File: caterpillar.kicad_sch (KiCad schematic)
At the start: 31 parts, among them J1 Conn_ARM_JTAG_SWD_10, M1 Conn_01x02_Pin, M2 *, M3 Conn_01x02_Pin, U1 STBB1-APUR, U2 ASM330LHHTR, U3 DRV8212P, U4 ADP2503ACPZ-3.3-R7, U6 max5419leta+T

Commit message: library: extract AN54LQ-P15 module from design files into a real library
The Raytac AN54LQ-P15 (nRF54L15) module existed only as embedded copies
in the schematic/board; its source library was a broken absolute path
on another machine. Extract it into library/AN54LQ-P15/ per the
project's component layout:

- footprint: pulled from the placed M2 via the pcbnew API (position
  reset, REF**, nets/sheet path stripped), 41 pads verified
- symbol: extracted from the schematic's lib_symbols, wrapped as a
  KiCad 10 symbol library, Footprint property fully qualified
- both lib tables gain an AN54LQ-P15 entry; nickname matches existing
  design references, so no design-file changes needed
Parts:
- U1: footprint STBB1_APUR:SON_B1-APUR_STM -> SON_B1-APUR_STM
- U2: footprint ASM330LHHTR:LGA-14L_2P5X3X0P83_STM -> LGA-14L_2P5X3X0P83_STM
- U4: footprint ADP2503ACPZ_3_3_R7:CP_10_9_ADI -> CP_10_9_ADI
- U6: footprint max5419:21-0137_T833&plus_2_MXM-L -> 21-0137_T833+2_MXM
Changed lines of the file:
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@@
 			)
 		)
-		(property "Description" ""
+		(property "Description" "Inductor, small symbol"
 			(at 40.64 149.86 90)
 			(hide yes)
@@
 			)
 		)
-		(property "Description" ""
+		(property "Description" "Generic connector, single row, 01x01, script generated"
 			(at 238.76 143.51 0)
 			(hide yes)
@@
 			)
 		)
-		(property "Description" ""
+		(property "Description" "Unpolarized capacitor, small symbol"
 			(at 220.98 124.46 0)
 			(hide yes)
@@
 			)
 		)
-		(property "Description" ""
+		(property "Description" "Unpolarized capacitor, small symbol"
 			(at 44.45 142.24 0)
 			(hide yes)
@@
 			)
 		)
-		(property "Description" ""
+		(property "Description" "Resistor, small US symbol"
 			(at 213.36 125.73 0)
 			(hide yes)
@@
 			)
 		)
-		(property "Description" ""
+		(property "Description" "Generic connector, single row, 01x02, script generated"
 			(at 17.78 154.94 0)
 			(hide yes)
@@
 			)
 		)
-		(property "Description" ""
+		(property "Description" "Unpolarized capacitor, small symbol"
 			(at 138.43 144.78 0)
 			(hide yes)
@@
 			)
 		)
-		(property "Description" ""
+		(property "Description" "Generic connector, single row, 01x01, script generated"
 			(at 238.76 146.05 0)
 			(hide yes)
@@
 			)
 		)
-		(property "Description" ""
+		(property "Description" "Generic connector, single row, 01x02, script generated"
 			(at 24.13 92.71 0)
 			(hide yes)
@@
 			)
 		)
-		(property "Description" ""
+		(property "Description" "Inductor, small symbol"
 			(at 137.16 138.43 90)
 			(hide yes)
@@
 			)
 		)
-		(property "Description" ""
+		(property "Description" "Resistor, small US symbol"
 			(at 231.14 128.27 0)
 			(hide yes)
@@
 			)
 		)
-		(property "Description" ""
+		(property "Description" "Unpolarized capacitor, small symbol"
 			(at 257.81 87.63 0)
 			(hide yes)
@@
 			)
 		)
-		(property "Footprint" "max5419:21-0137_T833&plus_2_MXM-L"
+		(property "Footprint" "21-0137_T833+2_MXM"
 			(at 125.73 179.07 0)
 			(hide yes)
@@
 			)
 		)
-		(property "Description" ""
+		(property "Description" "Unpolarized capacitor, small symbol"
 			(at 261.62 87.63 0)
 			(hide yes)
@@
 			)
 		)
-		(property "Description" ""
+		(property "Description" "Unpolarized capacitor, small symbol"
 			(at 142.24 127 0)
 			(hide yes)
@@
 			)
 		)
-		(property "Description" ""
+		(property "Description" "Generic connector, single row, 01x01, script generated"
 			(at 238.76 148.59 0)
 			(hide yes)
@@
 			)
 		)
-		(property "Description" ""
+		(property "Description" "Unpolarized capacitor, small symbol"
 			(at 16.51 132.08 0)
 			(hide yes)
@@
 			)
 		)
-		(property "Footprint" "ASM330LHHTR:LGA-14L_2P5X3X0P83_STM"
+		(property "Footprint" "LGA-14L_2P5X3X0P83_STM"
 			(at 212.09 69.85 0)
 			(hide yes)
@@
 			)
 		)
-		(property "Footprint" "ADP2503ACPZ_3_3_R7:CP_10_9_ADI"
+		(property "Footprint" "CP_10_9_ADI"
 			(at 48.26 144.78 0)
 			(hide yes)
@@
 			)
 		)
-		(property "Footprint" "STBB1_APUR:SON_B1-APUR_STM"
+		(property "Footprint" "SON_B1-APUR_STM"
 			(at 144.78 132.08 0)
 			(hide yes)
@@
 			)
 		)
-		(property "Description" ""
+		(property "Description" "Resistor, small US symbol"
 			(at 238.76 128.27 0)
 			(hide yes)
@@
 			)
 		)
-		(property "Description" ""
+		(property "Description" "Generic connector, single row, 01x01, script generated"
 			(at 238.76 151.13 0)
 			(hide yes)
@@
 			)
 		)
-		(property "Description" ""
+		(property "Description" "Unpolarized capacitor, small symbol"
 			(at 125.73 175.26 0)
 			(hide yes)

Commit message: replaced L5 with large inductor footprints. Fixed some warning about footprint links. Using M (largest pads) footprints for ICs now
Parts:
- L5: footprint Inductor_SMD:L_0402_1005Metric -> VLCF4020T-2R2N1R7:VLCF4020
- U1: footprint SON_B1-APUR_STM -> STBB1_APUR:SON_B1-APUR_STM-M
- U2: footprint LGA-14L_2P5X3X0P83_STM -> ASM330LHHTR:LGA-14L_2P5X3X0P83_STM-L
- U4: footprint CP_10_9_ADI -> ADP2503ACPZ_3_3_R7:CP_10_9_ADI-M
- U6: footprint 21-0137_T833+2_MXM -> max5419:21-0137_T833&plus_2_MXM-M
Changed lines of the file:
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@@
 			)
 		)
-		(property "Footprint" "Inductor_SMD:L_0402_1005Metric"
+		(property "Footprint" "VLCF4020T-2R2N1R7:VLCF4020"
 			(at 137.16 138.43 0)
 			(hide yes)
@@
 			)
 		)
-		(property "Footprint" "21-0137_T833+2_MXM"
+		(property "Footprint" "max5419:21-0137_T833&plus_2_MXM-M"
 			(at 125.73 179.07 0)
 			(hide yes)
@@
 			)
 		)
-		(property "Footprint" "LGA-14L_2P5X3X0P83_STM"
+		(property "Footprint" "ASM330LHHTR:LGA-14L_2P5X3X0P83_STM-L"
 			(at 212.09 69.85 0)
 			(hide yes)
@@
 			)
 		)
-		(property "Footprint" "CP_10_9_ADI"
+		(property "Footprint" "ADP2503ACPZ_3_3_R7:CP_10_9_ADI-M"
 			(at 48.26 144.78 0)
 			(hide yes)
@@
 			)
 		)
-		(property "Footprint" "SON_B1-APUR_STM"
+		(property "Footprint" "STBB1_APUR:SON_B1-APUR_STM-M"
 			(at 144.78 132.08 0)
 			(hide yes)

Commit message: replaced all 0402 footprints with 0603
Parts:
- C1, C10, C11, C12, C2, C3, C5, C6, C7, C8, C9: footprint Capacitor_SMD:C_0402_1005Metric -> Capacitor_SMD:C_0603_1608Metric
- L1, L6: footprint Inductor_SMD:L_0402_1005Metric -> Inductor_SMD:L_0603_1608Metric
- R3, R4, R8: footprint Resistor_SMD:R_0402_1005Metric -> Resistor_SMD:R_0603_1608Metric
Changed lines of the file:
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@@
 			)
 		)
-		(property "Footprint" "Inductor_SMD:L_0402_1005Metric"
+		(property "Footprint" "Inductor_SMD:L_0603_1608Metric"
 			(at 40.64 149.86 0)
 			(hide yes)
@@
 			)
 		)
-		(property "Footprint" "Capacitor_SMD:C_0402_1005Metric"
+		(property "Footprint" "Capacitor_SMD:C_0603_1608Metric"
 			(at 220.98 124.46 0)
 			(hide yes)
@@
 			)
 		)
-		(property "Footprint" "Capacitor_SMD:C_0402_1005Metric"
+		(property "Footprint" "Capacitor_SMD:C_0603_1608Metric"
 			(at 44.45 142.24 0)
 			(hide yes)
@@
 			)
 		)
-		(property "Footprint" "Resistor_SMD:R_0402_1005Metric"
+		(property "Footprint" "Resistor_SMD:R_0603_1608Metric"
 			(at 213.36 125.73 0)
 			(hide yes)
@@
 			)
 		)
-		(property "Footprint" "Capacitor_SMD:C_0402_1005Metric"
+		(property "Footprint" "Capacitor_SMD:C_0603_1608Metric"
 			(at 138.43 144.78 0)
 			(hide yes)
@@
 			)
 		)
-		(property "Footprint" "Capacitor_SMD:C_0402_1005Metric"
+		(property "Footprint" "Capacitor_SMD:C_0603_1608Metric"
 			(at 72.39 35.56 0)
 			(hide yes)
@@
 			)
 		)
-		(property "Footprint" "Capacitor_SMD:C_0402_1005Metric"
+		(property "Footprint" "Capacitor_SMD:C_0603_1608Metric"
 			(at 66.04 35.56 0)
 			(hide yes)
@@
 			)
 		)
-		(property "Footprint" "Capacitor_SMD:C_0402_1005Metric"
+		(property "Footprint" "Capacitor_SMD:C_0603_1608Metric"
 			(at 58.42 35.56 0)
 			(hide yes)
@@
 			)
 		)
-		(property "Footprint" "Resistor_SMD:R_0402_1005Metric"
+		(property "Footprint" "Resistor_SMD:R_0603_1608Metric"
 			(at 231.14 128.27 0)
 			(hide yes)
@@
 			)
 		)
-		(property "Footprint" "Capacitor_SMD:C_0402_1005Metric"
+		(property "Footprint" "Capacitor_SMD:C_0603_1608Metric"
 			(at 257.81 87.63 0)
 			(hide yes)
@@
 			)
 		)
-		(property "Footprint" "Capacitor_SMD:C_0402_1005Metric"
+		(property "Footprint" "Capacitor_SMD:C_0603_1608Metric"
 			(at 261.62 87.63 0)
 			(hide yes)
@@
 			)
 		)
-		(property "Footprint" "Inductor_SMD:L_0402_1005Metric"
+		(property "Footprint" "Inductor_SMD:L_0603_1608Metric"
 			(at 114.3 63.5 0)
 			(hide yes)
@@
 			)
 		)
-		(property "Footprint" "Capacitor_SMD:C_0402_1005Metric"
+		(property "Footprint" "Capacitor_SMD:C_0603_1608Metric"
 			(at 142.24 127 0)
 			(hide yes)
@@
 			)
 		)
-		(property "Footprint" "Capacitor_SMD:C_0402_1005Metric"
+		(property "Footprint" "Capacitor_SMD:C_0603_1608Metric"
 			(at 16.51 132.08 0)
 			(hide yes)
@@
 			)
 		)
-		(property "Footprint" "Resistor_SMD:R_0402_1005Metric"
+		(property "Footprint" "Resistor_SMD:R_0603_1608Metric"
 			(at 238.76 128.27 0)
 			(hide yes)
@@
 			)
 		)
-		(property "Footprint" "Capacitor_SMD:C_0402_1005Metric"
+		(property "Footprint" "Capacitor_SMD:C_0603_1608Metric"
 			(at 125.73 175.26 0)
 			(hide yes)

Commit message: reorganized design a lot for better space organization
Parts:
- removed 3.3V1, GND2, SCL1, SDA1: Conn_01x01_Pin, Connector_Wire:SolderWirePad_1x01_SMD_1x2mm, symbol Connector:Conn_01x01_Pin
- removed M1: Conn_01x02_Pin, Connector_PinHeader_2.00mm:PinHeader_1x02_P2.00mm_Vertical, symbol Connector:Conn_01x02_Pin
- removed M3: Conn_01x02_Pin, Connector_PinHeader_2.54mm:PinHeader_1x02_P2.54mm_Vertical, symbol Connector:Conn_01x02_Pin
- added J2: SM02B-SRSS-TB_LF__SN_, SM02B-SRSS-TB:SM02BSRSSTBLFSN, symbol SM02B-SRSS-TB:SM02B-SRSS-TB_LF__SN_
- added J3, J4: Castellated_2PTH_P1.27mm, Castellated_2PTH_P1.27mm:Castellated_2PTH_P1.27mm, symbol Castellated_2PTH_P1.27mm:Castellated_2PTH_P1.27mm
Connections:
- net +BATT: now also J2.1
- net GND: now also J2.2
- net OUT1: now also J3.1
- net OUT2: now also J4.1
- no-connect marks 5 -> 7

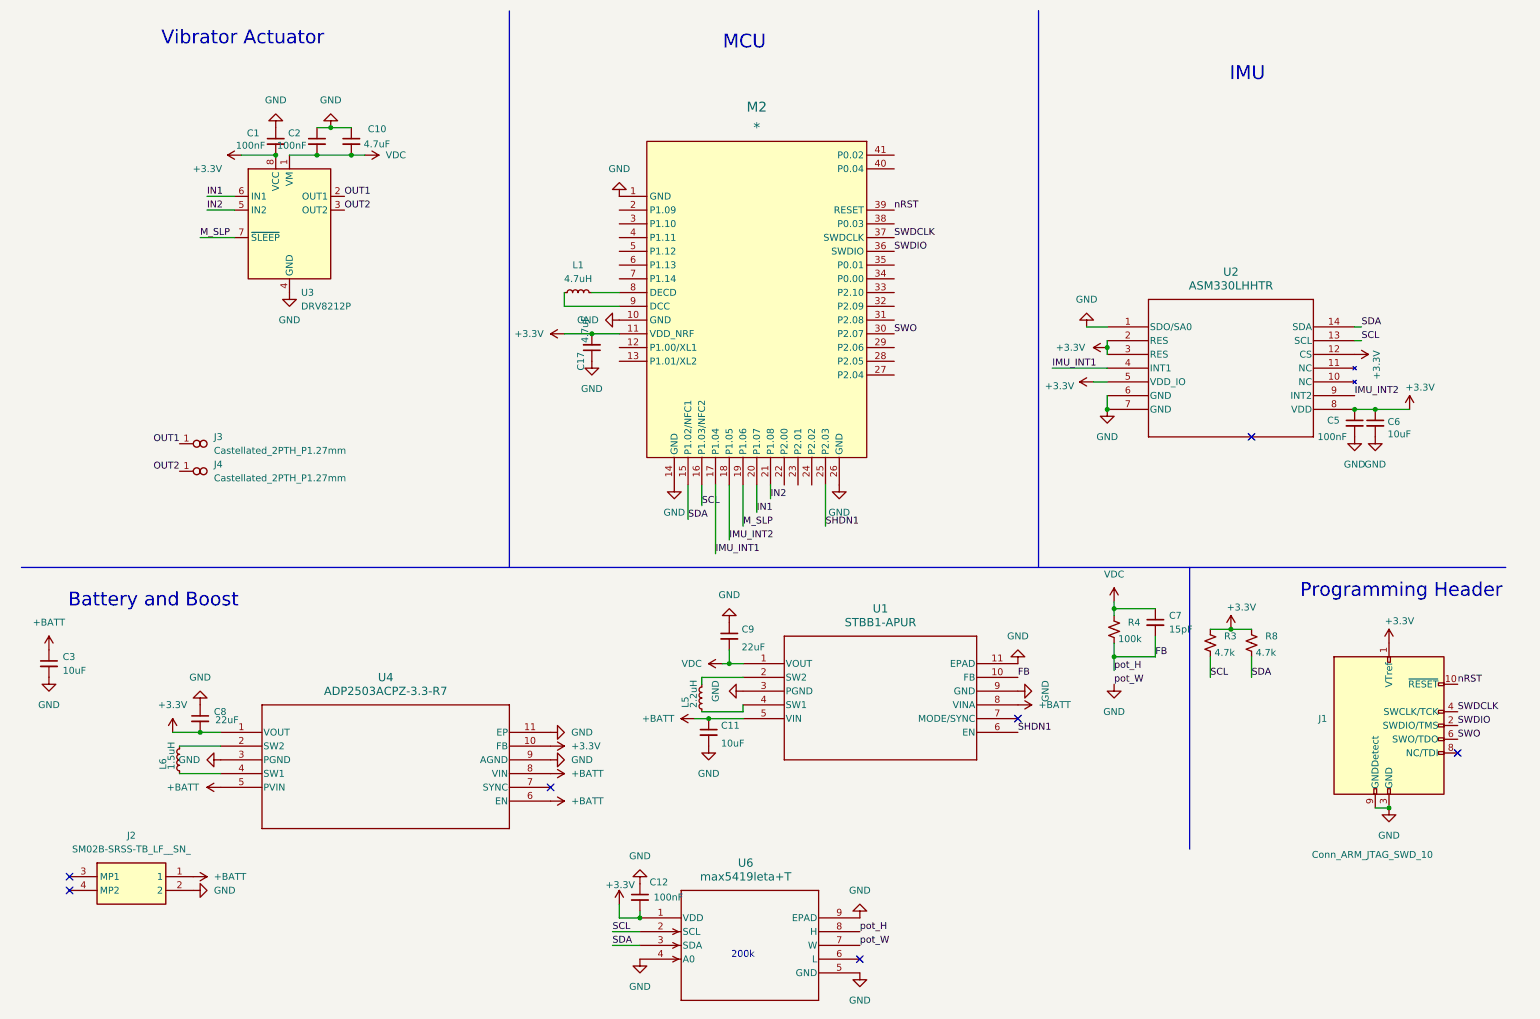
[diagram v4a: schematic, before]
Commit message: sch: move IMU to dedicated SPI; I2C stays for digipot; decoupling fixes
- ASM330LHHTR now on SPI: CS=P1.09, SCLK=P1.10, MOSI=P1.13, MISO=P1.14
  (SDO/SA0 repurposed from I2C address strap to MISO)
- I2C bus (P1.02/P1.03 + pull-ups) retained for MAX5419 digipot only
- C6 repurposed 10uF -> 100nF as the IMU VDD_IO ceramic that the
  datasheet requires; bulk duty covered by C8 22uF, 3.2mm away
- ADP2503 SYNC pin grounded (was floating) -> auto power-save mode
- README pin map updated to match

Firmware devicetree (boards/kamoamoa/caterpillar/) still describes the
IMU on I2C - must be updated to SPI with these pins before next flash.
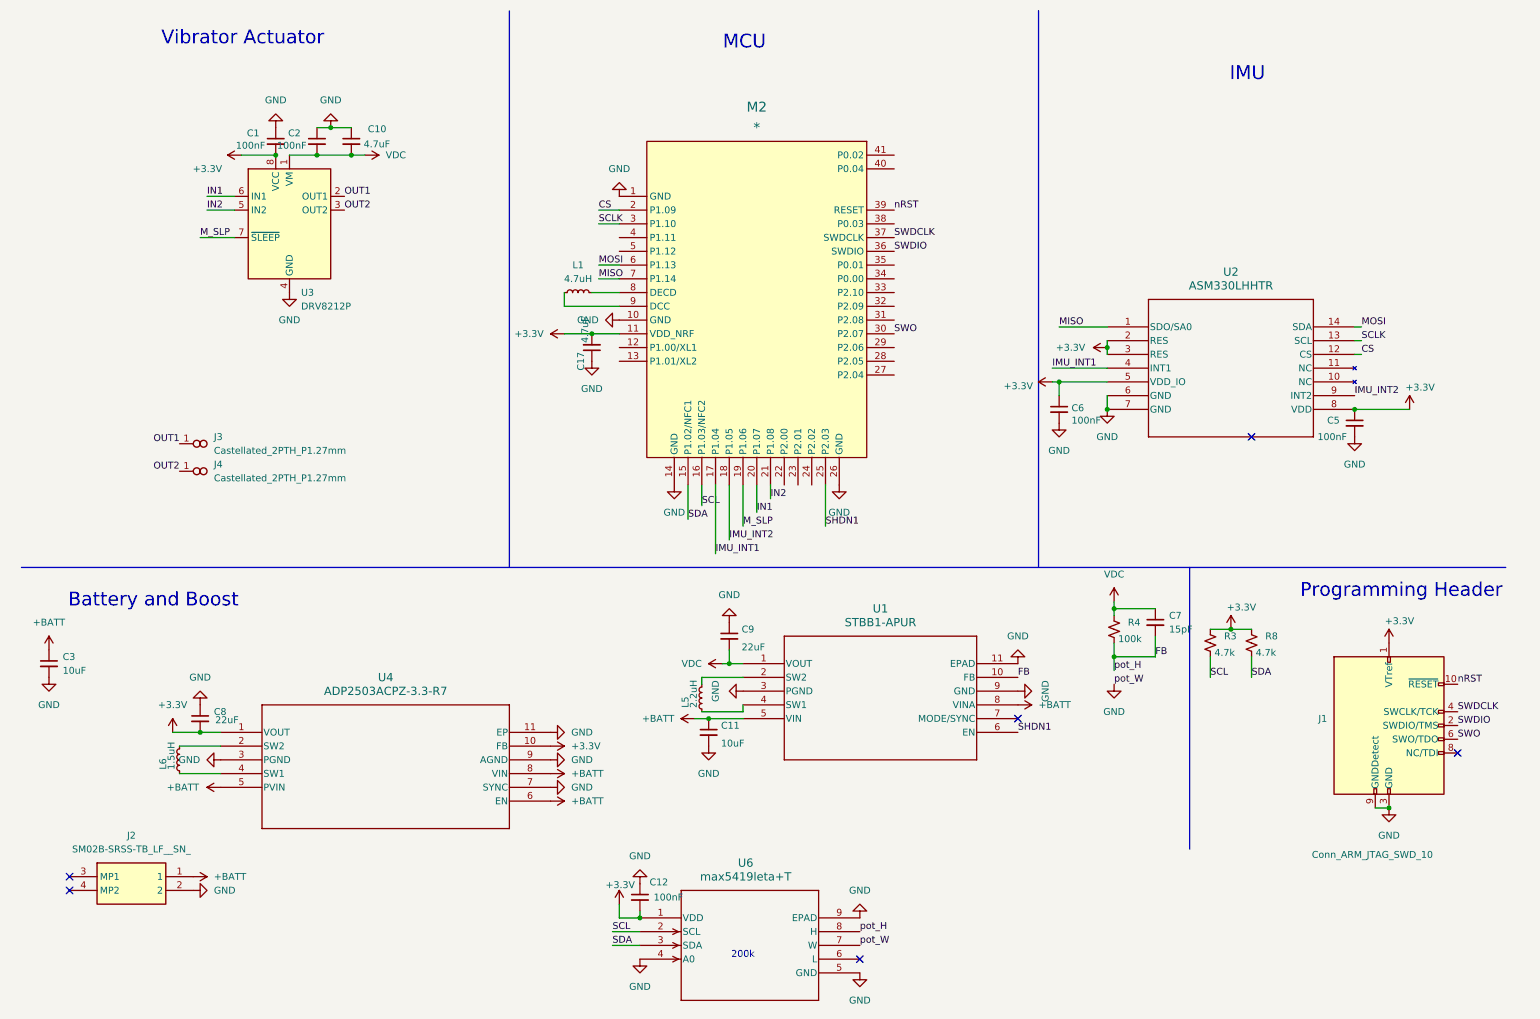
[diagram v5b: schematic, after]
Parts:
- C6: value 10uF -> 100nF
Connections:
- net +3.3V: no longer U2.12 (CS)
- net GND: now also U4.7 (SYNC); no longer U2.1 (SDO/SA0)
- net SCL: no longer U2.13 (SCL)
- net SDA: no longer U2.14 (SDA)
- net CS: now reaches M2.2 (P1.09)
- net CS: now also U2.12 (CS)
- net SCLK: now reaches M2.3 (P1.10)
- net SCLK: now also U2.13 (SCL)
- net MOSI: now reaches M2.6 (P1.13)
- net MOSI: now also U2.14 (SDA)
- net MISO: now reaches M2.7 (P1.14)
- net MISO: now also U2.1 (SDO/SA0)
- no-connect marks 7 -> 6

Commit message: sch: add VDC sense divider on P1.11; ground STBB1 MODE/SYNC; tidy power drawing
- VDC telemetry: 100k/100k divider (/2) + 100nF filter (32Hz) into
  P1.11 SAADC; measures the digipot-set motor rail, ~22uA drain,
  quasi-static readings only by design (wait ~25ms after setpoint
  changes). Verify P1.11 is an AIN pin before fab.
- STBB1 MODE/SYNC grounded (was floating) -> auto power-save, matches
  ADP2503 SYNC treatment
- C3 redrawn at ADP2503 VIN for clarity (electrically unchanged);
  redundant +BATT symbol replaced with wires

PENDING on the board: run Update PCB from Schematic WITH the
"re-link by reference designator" option (repairs C3/C6 uuid links
broken by delete-and-redraw) and place new C13/R5/R6.
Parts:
- added C13: 100nF, Capacitor_SMD:C_0603_1608Metric, symbol Device:C_Small
- added R5, R6: 100k, Resistor_SMD:R_0603_1608Metric, symbol Device:R_Small_US
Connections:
- net GND: now also U1.7 (MODE/SYNC), C13.2, R5.1
- net VDC: now also R6.2
- net VDC_SENSE: now reaches M2.4 (P1.11)
- net VDC_SENSE: now also C13.1, R5.2, R6.1
- no-connect marks 6 -> 5

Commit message: sch: motor-rail safety nets - EN pulldown, hardware VDC ceiling; drop C7
- R7 100k pulldown on STBB1 EN (/SHDN1): rail guaranteed off while
  the MCU is in reset/bootloader/flashing (GPIO hi-Z)
- R9 12.1k in series between MAX5419 H terminal and STBB1 FB:
  hardware VDC ceiling = 0.5*(1+100k/12.1k) ~= 4.63V regardless of
  firmware/BLE commands; max commandable ~4.3-4.5V (wiper R dependent)
- C7 15pF feedforward cap removed (owner decision): STBB1 eval board
  ships without one, and R9 now floors the FB bottom leg at high
  frequency, damping the digipot-parasitic pole C7 likely compensated.
  Verify with a scope on VDC (digipot sweep + motor start) on first
  new build.

Firmware ripple: digipot tap<->voltage constants must include R9.

Board still pending one Update-PCB-from-Schematic run with BOTH
"re-link by reference" (C3/C6 uuids) and "delete footprints with no
symbols" (orphan C7 footprint) checked, then place R7/R9/C13/R5/R6.
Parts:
- removed C7: 15pF, Capacitor_SMD:C_0603_1608Metric, symbol Device:C_Small
- added R7: 100k, Resistor_SMD:R_0603_1608Metric, symbol Device:R_Small_US
- added R9: 12.1k, Resistor_SMD:R_0603_1608Metric, symbol Device:R_Small_US
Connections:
- net FB: now also R9.1; no longer U6.8 (H)
- net GND: now also R7.1
- net SHDN1: now also R7.2
- new net pot_H: R9.2, U6.8 (H)

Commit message: pcb: sync with rev-2 schematic; bom: regenerate with MPN fields
- Board updated from schematic (re-linked by reference): C3/C6 uuid
  links repaired, orphan C7 footprint removed, R7/R9/C13/R5/R6 placed
  onto the board (placement/routing to follow)
- BOM regenerated from the current schematic (old caterpillar.csv was
  a stale Muscle_PCB-era export); grouped by value+footprint
- MPN stored as symbol fields in the schematic so BOM exports carry
  them automatically: C3/C11=GMC10X7R106K10NT (10uF 10V X7R 0603),
  C8/C9=CL10A226MP8NUNE (22uF 10V X5R 0603, DC-bias headroom for
  4.63V VDC), L6=LSCNB1608HKT1R5MD (1.5uH 1.3A 0603)
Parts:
- C11, C3: MPN (none) -> GMC10X7R106K10NT
- C8, C9: MPN (none) -> CL10A226MP8NUNE
- L6: MPN (none) -> LSCNB1608HKT1R5MD
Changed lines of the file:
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@@
 			)
 		)
+		(property "MPN" "LSCNB1608HKT1R5MD"
+			(at 40.64 149.86 0)
+			(show_name no)
+			(do_not_autoplace no)
+			(hide yes)
+			(effects
+				(font
+					(size 1.27 1.27)
+				)
+			)
+		)
 		(property "Description" "Inductor, small symbol"
 			(at 40.64 149.86 90)
@@
 			)
 		)
+		(property "MPN" "CL10A226MP8NUNE"
+			(at 44.45 142.24 0)
+			(show_name no)
+			(do_not_autoplace no)
+			(hide yes)
+			(effects
+				(font
+					(size 1.27 1.27)
+				)
+			)
+		)
 		(property "Description" "Unpolarized capacitor, small symbol"
 			(at 44.45 142.24 0)
@@
 			)
 		)
+		(property "MPN" "GMC10X7R106K10NT"
+			(at 138.43 144.78 0)
+			(show_name no)
+			(do_not_autoplace no)
+			(hide yes)
+			(effects
+				(font
+					(size 1.27 1.27)
+				)
+			)
+		)
 		(property "Description" "Unpolarized capacitor, small symbol"
 			(at 138.43 144.78 0)
@@
 			)
 		)
+		(property "MPN" "CL10A226MP8NUNE"
+			(at 142.24 127 0)
+			(show_name no)
+			(do_not_autoplace no)
+			(hide yes)
+			(effects
+				(font
+					(size 1.27 1.27)
+				)
+			)
+		)
 		(property "Description" "Unpolarized capacitor, small symbol"
 			(at 142.24 127 0)
@@
 			(effects
 				(font
+					(size 1.27 1.27)
+				)
+			)
+		)
+		(property "MPN" "GMC10X7R106K10NT"
+			(at 121.92 154.94 0)
+			(show_name no)
+			(do_not_autoplace no)
+			(hide yes)
+			(effects
+				(font
